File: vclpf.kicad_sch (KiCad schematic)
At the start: 41 parts, among them J1 NJ2FD-V, J2 NJ2FD-V, J3 NJ2FD-V, Q1 2N3904, Q2 2N3906, Q3 2N3904, Q4 2N3906, U1 ADA4084-4xCP, U2 ADA4084-4xCP

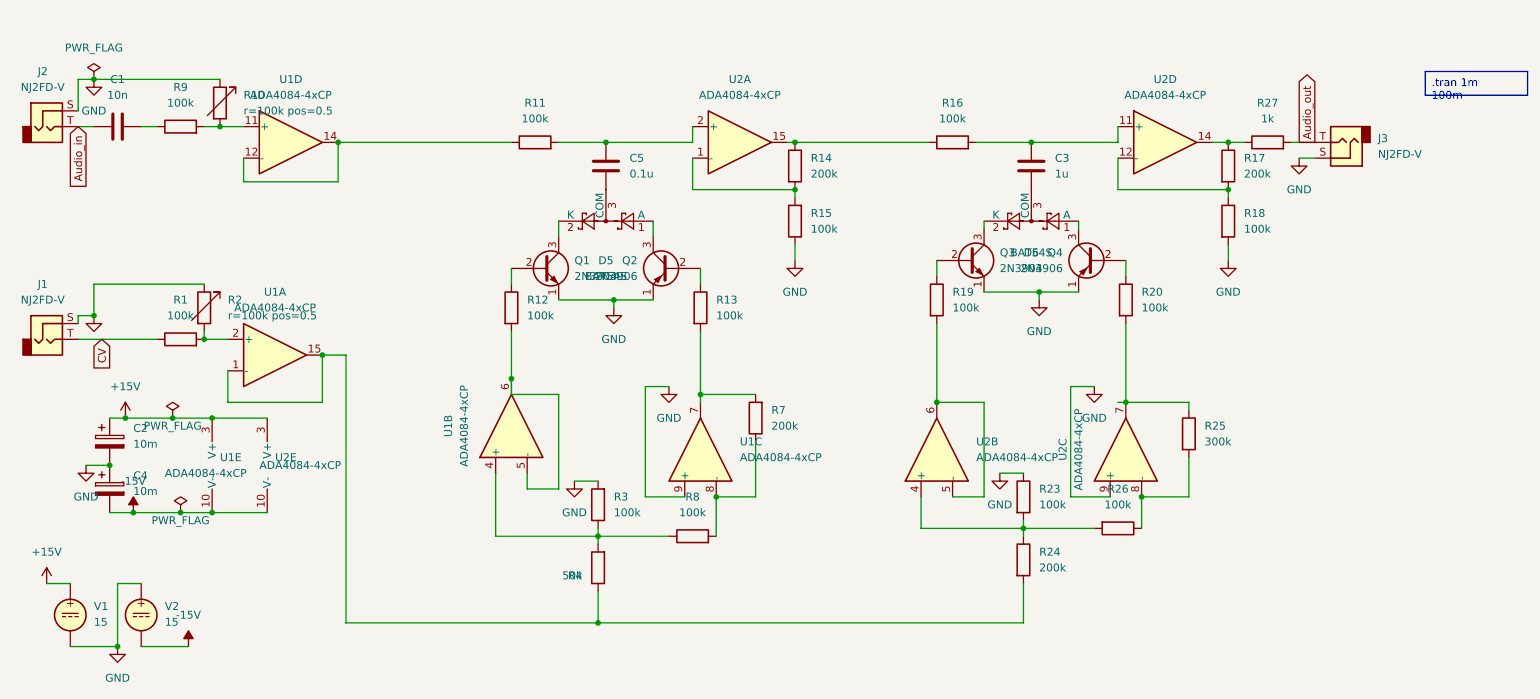
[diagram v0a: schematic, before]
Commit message: improved correktion amping
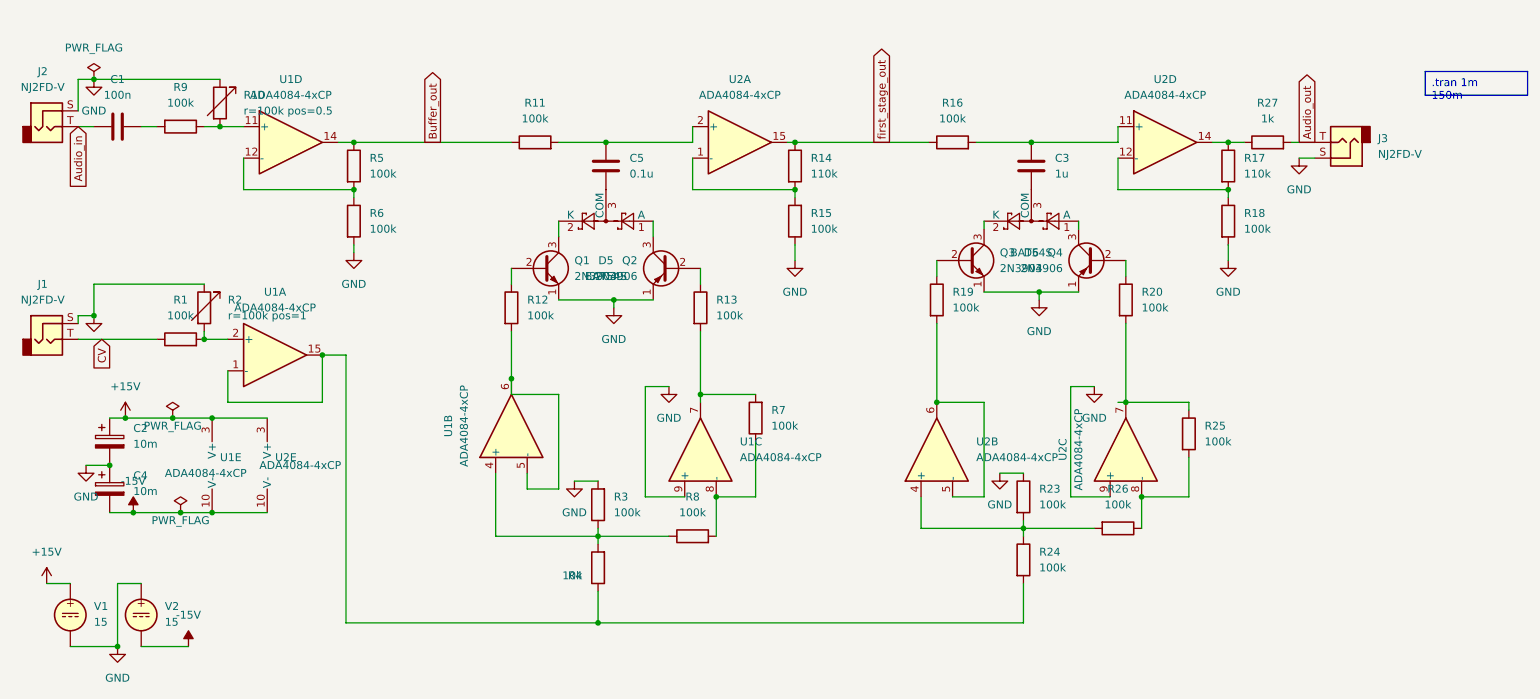
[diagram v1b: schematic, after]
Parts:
- added R5, R6: 100k, symbol Device:R
- C1: value 10n -> 100n
- R14, R17: value 200k -> 110k
- R24, R7: value 200k -> 100k
- R25: value 300k -> 100k
- R4: value 50k -> 10k
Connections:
- net GND: now also R6.2
- net at R9.1: now also R10.2, U1.11 (+); no longer C1.2
- net Buffer_out: now reaches R11.1, U1.14
- net Buffer_out: now also R5.1; no longer U1.12 (-)
- net first_stage_out: now reaches R14.1, R16.1, U2.15
- new net: C1.2, R9.2
- new net: R5.2, R6.1, U1.12 (-)
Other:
- moved on the sheet: R9
